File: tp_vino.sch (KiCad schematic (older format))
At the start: 11 parts, among them P3 UartSim, Q1 BC849, U7 SIM800L

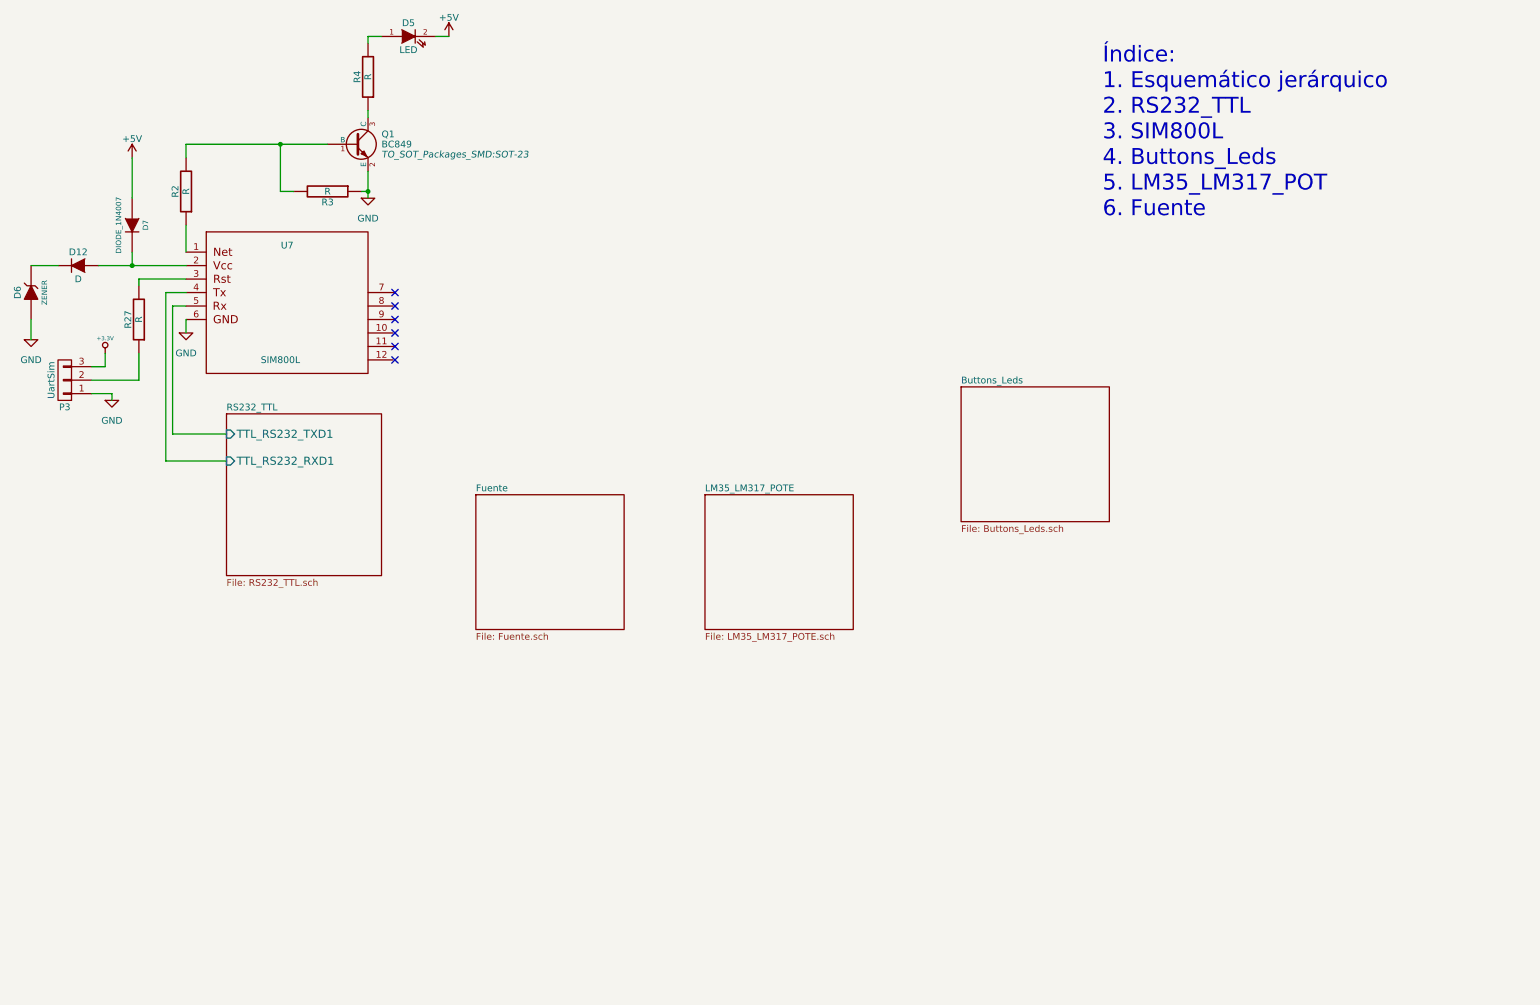
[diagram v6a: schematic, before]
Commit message: Add digikey code and comment schematic.
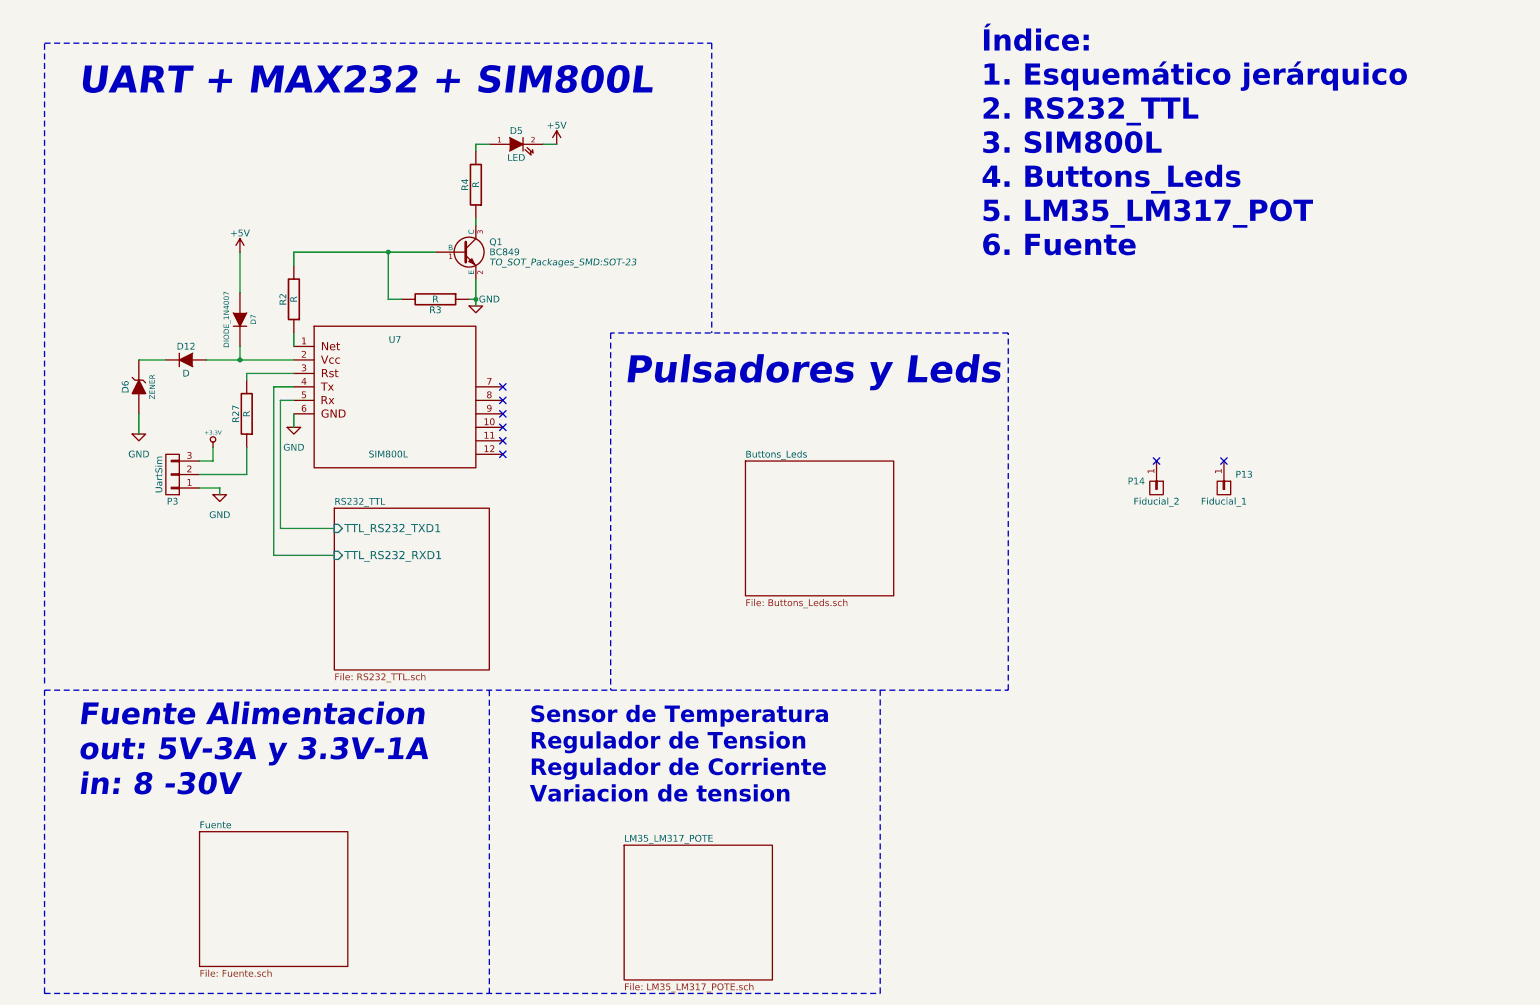
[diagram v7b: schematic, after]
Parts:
- added P13: Fiducial_1, symbol CONN_01X01
- added P14: Fiducial_2, symbol CONN_01X01
- D5: Digikey (none) -> SML-LX1206GC-TR SML-LX1206GC-TR
- Q1: Digikey# (none) -> BC849BLT1GOSTR-ND
- R2, R27, R3, R4: Digikey# (none) -> CRCW12060000Z0EA
- U7: Digikey# (none) -> 1471-1458-ND
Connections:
- no-connect marks 6 -> 8
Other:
- note added: "Fuente Alimentacion\nout: 5V-3A y 3.3V-1A\nin: 8 -30V \n"
- note added: "Pulsadores y Leds"
- note added: "Sensor de Temperatura\nRegulador de Tension\nRegulador de Corriente\nVariacion de tension"
- note added: "UART + MAX232 + SIM800L"
- moved on the sheet: D12, D5, D6, D7, P3, Q1, R2, R27, R3, R4, U7

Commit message: Actualizo las revisiones y documentaciones faltante. Algunas correcciones realizadas, faltan algunas mas que vere de hacerlas.
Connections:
- net +5V: now also D5.1 (A); no longer D5.2 (K)
- net at R4.2: now also D5.2 (K); no longer D5.1 (A)
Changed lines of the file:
@@
 F 4 "SML-LX1206GC-TR	SML-LX1206GC-TR" H 4200 1450 60  0001 C CNN "Digikey"
 	1    4200 1450
-	1    0    0    -1
+	-1   0    0    1
 $EndComp
 $Comp
